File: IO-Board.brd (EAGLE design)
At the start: 160 x 100 mm, 59 parts, among them IC1 PCF8574P, IC2 PCF8574P

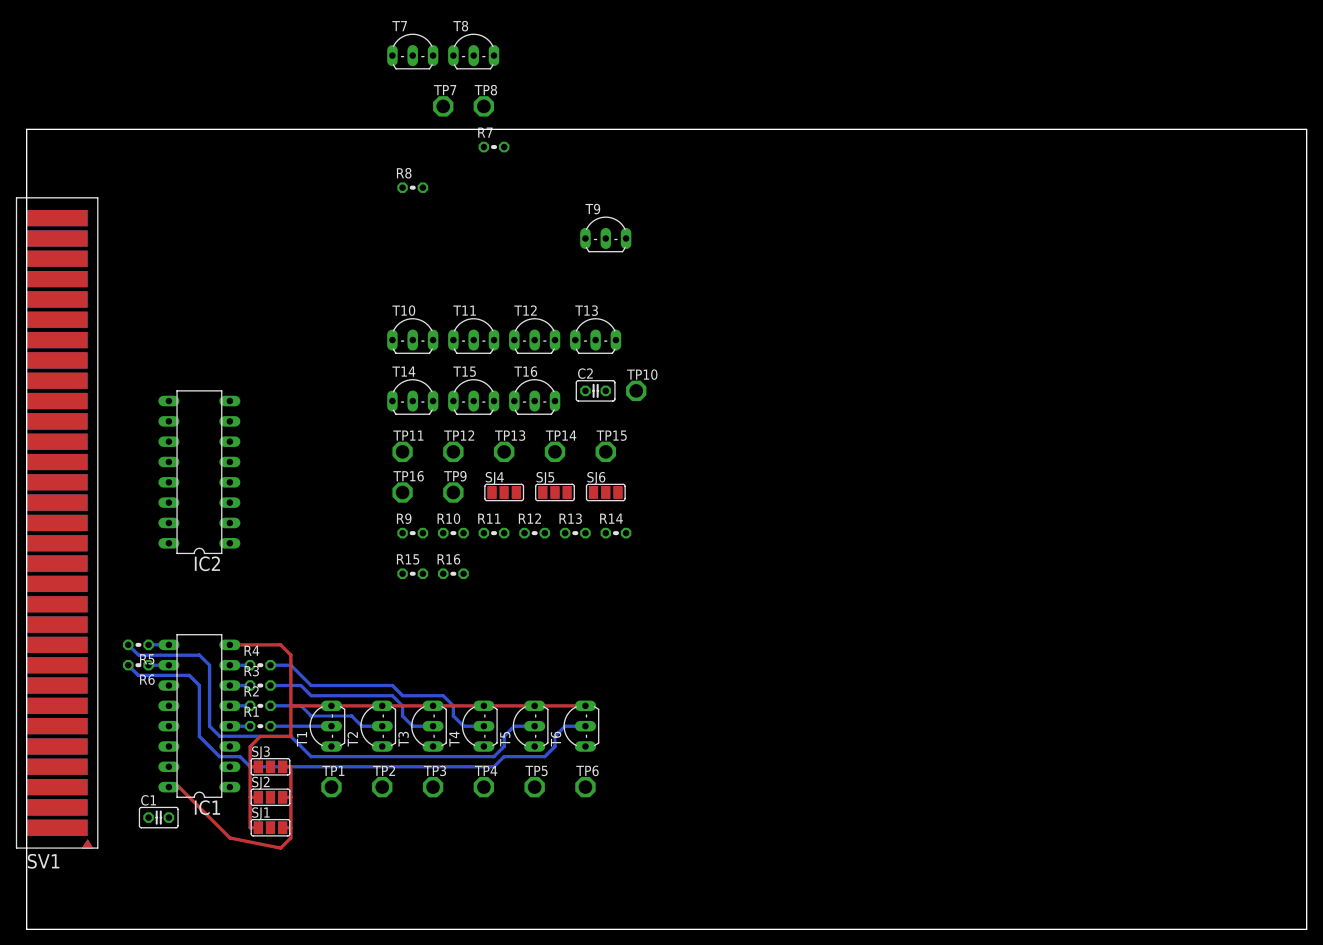
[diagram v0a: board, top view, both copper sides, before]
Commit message: IO-Board angepasst, 433MHz-Sender hinzugefügt
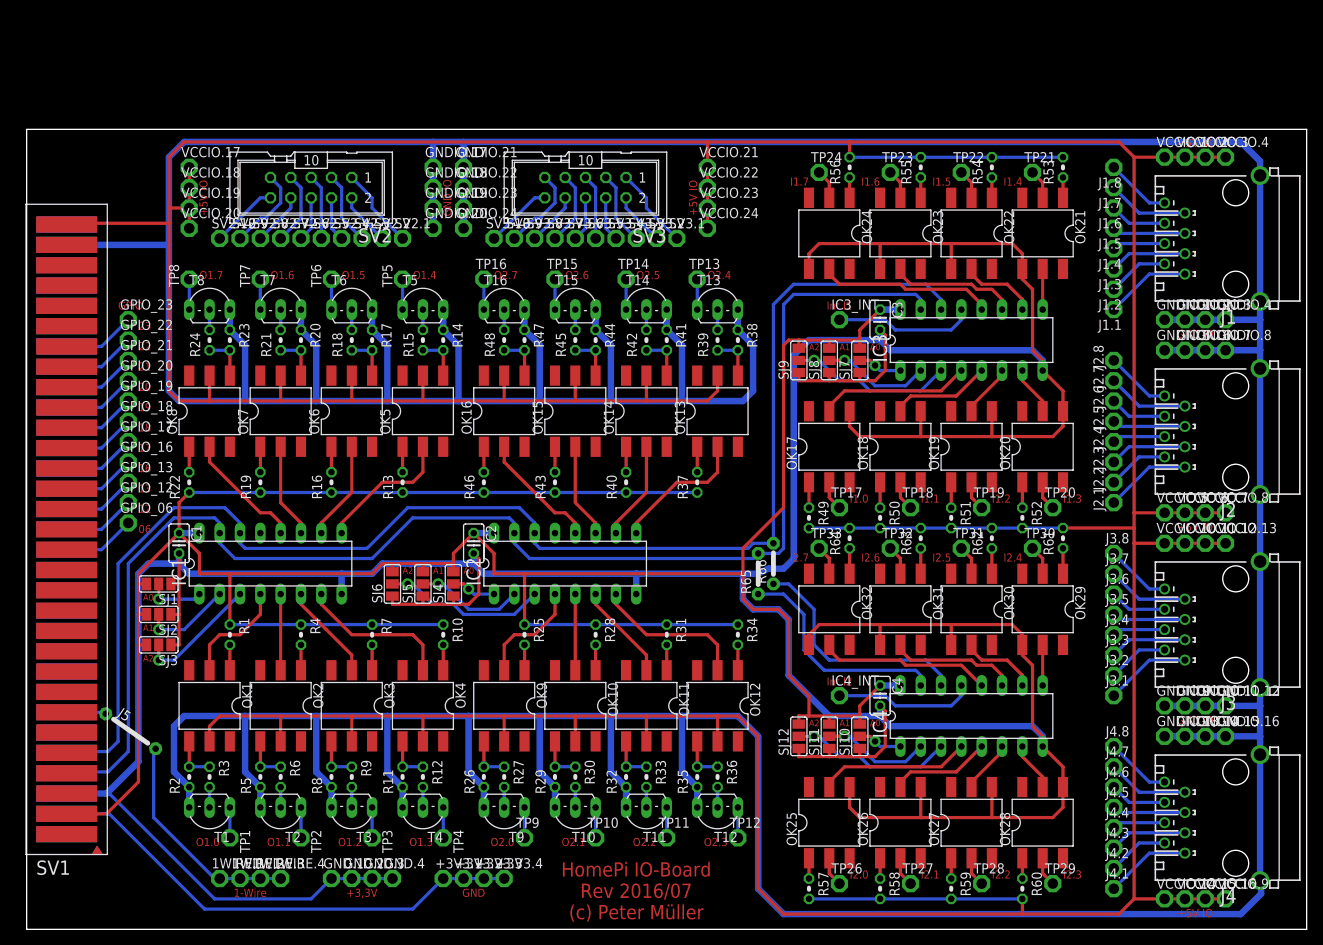
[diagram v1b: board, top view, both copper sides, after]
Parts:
- added +3V3.1, +3V3.2, +3V3.3, +3V3.4, 1WIRE.1, 1WIRE.2, 1WIRE.3, 1WIRE.4, GND.1, GND.2, GND.3, GND.4, GNDIO.1, GNDIO.10, GNDIO.11, GNDIO.12, GNDIO.13, GNDIO.14, GNDIO.15, GNDIO.16, GNDIO.17, GNDIO.18, GNDIO.19, GNDIO.2, GNDIO.20, GNDIO.21, GNDIO.22, GNDIO.23, GNDIO.24, GNDIO.3, GNDIO.4, GNDIO.5, GNDIO.6, GNDIO.7, GNDIO.8, GNDIO.9, GPIO_06, GPIO_12, GPIO_13, GPIO_16, GPIO_17, GPIO_18, GPIO_19, GPIO_20, GPIO_21, GPIO_22, GPIO_23, IC3_INT, IC4_INT, J1.1, J1.2, J1.3, J1.4, J1.5, J1.6, J1.7, J1.8, J2.1, J2.2, J2.3, J2.4, J2.5, J2.6, J2.7, J2.8, J3.1, J3.2, J3.3, J3.4, J3.5, J3.6, J3.7, J3.8, J4.1, J4.2, J4.3, J4.4, J4.5, J4.6, J4.7, J4.8, SV2.1, SV2.10, SV2.2, SV2.3, SV2.4, SV2.5, SV2.6, SV2.7, SV2.8, SV2.9, SV3.1, SV3.10, SV3.2, SV3.3, SV3.4, SV3.5, SV3.6, SV3.7, SV3.8, SV3.9, TP17, TP18, TP19, TP20, TP21, TP22, TP23, TP24, TP26, TP27, TP28, TP29, TP30, TP31, TP32, TP33, VCCIO.1, VCCIO.10, VCCIO.11, VCCIO.12, VCCIO.13, VCCIO.14, VCCIO.15, VCCIO.16, VCCIO.17, VCCIO.18, VCCIO.19, VCCIO.2, VCCIO.20, VCCIO.21, VCCIO.22, VCCIO.23, VCCIO.24, VCCIO.3, VCCIO.4, VCCIO.5, VCCIO.6, VCCIO.7, VCCIO.8, VCCIO.9: TPPAD1-13, testpad:P1-13
- added C3, C4: 100nF, rcl:C025-025X050
- added IC3, IC4: PCF8574P, micro-philips:DIL16
- added J1, J2, J3, J4: (no value), con-amp:555153-1
- added J5: J7MM, jumper:07
- added OK1, OK10, OK11, OK12, OK13, OK14, OK15, OK16, OK17, OK18, OK19, OK2, OK20, OK21, OK22, OK23, OK24, OK25, OK26, OK27, OK28, OK29, OK3, OK30, OK31, OK32, OK4, OK5, OK6, OK7, OK8, OK9: CNY17SMD, homepi:DIL06_SMD
- added R17, R20, R23, R26, R29, R32, R35, R38, R41, R44, R47: 10k, rcl:0204V
- added R18, R21, R24, R27, R30, R33, R36, R39, R42, R45, R48: 4k7, rcl:0204V
- added R19, R22, R25, R28, R31, R34, R37, R40, R43, R46, R49, R50, R51, R52, R53, R54, R55, R56, R57, R58, R59, R60, R61, R62, R63, R64: 330, rcl:0204V
- added R65, R66: J5MM, jumper:05
- added SJ10, SJ11, SJ12, SJ7, SJ8, SJ9: (no value), jumper:SJ_2
- added SV2, SV3: (no value), con-harting-ml:ML10
- R1, R10, R13, R16, R4, R7: value (none) -> 330
- R11, R14, R2, R5, R8: value (none) -> 10k
- R12, R15, R3, R6, R9: value (none) -> 4k7
- T1, T10, T11, T12, T13, T14, T15, T16, T2, T3, T4, T5, T6, T7, T8, T9: value (none) -> BC337-25; device transistor:TO92-EBC -> transistor:TO92-CBE
- TP1, TP10, TP11, TP12, TP13, TP14, TP15, TP16, TP2, TP3, TP4, TP5, TP6, TP7, TP8, TP9: value TPPAD1-17 -> TPPAD1-13; device testpad:P1-17 -> testpad:P1-13
- moved R8 74.4 mm to (38.1, 19.1), turned to 90 degrees
- moved T9 73.5 mm to (59.7, 15.2), turned to 180 degrees
- moved TP6 71.0 mm to (38.1, 81.3), turned to 90 degrees
- moved TP5 65.6 mm to (47.0, 81.3), turned to 90 degrees
- moved T12 63.9 mm to (86.4, 15.2), turned to 180 degrees
- moved T11 63.5 mm to (77.5, 15.2), turned to 180 degrees
- moved T10 63.1 mm to (68.6, 15.2), turned to 180 degrees
- moved R7 62.8 mm to (43.2, 36.8), turned to 270 degrees
- moved TP12 59.9 mm to (88.9, 11.4)
- moved T6 59.1 mm to (40.6, 77.5), turned to 0 degrees
- moved TP11 58.5 mm to (80.0, 11.4)
- moved TP10 56.1 mm to (71.1, 11.4)
- moved T5 53.6 mm to (49.5, 77.5), turned to 0 degrees
- moved IC2 47.1 mm to (67.3, 45.7), turned to 0 degrees
- moved T8 46.7 mm to (22.9, 77.5)
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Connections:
- removed net +5V: SV1.1, SV1.1T
- new net 1WIRE: 1WIRE.1.TP, 1WIRE.2.TP, 1WIRE.3.TP, 1WIRE.4.TP, J5.2
- new net GNDIO: GNDIO.1.TP, GNDIO.10.TP, GNDIO.11.TP, GNDIO.12.TP, GNDIO.13.TP, GNDIO.14.TP, GNDIO.15.TP, GNDIO.16.TP, GNDIO.17.TP, GNDIO.18.TP, GNDIO.19.TP, GNDIO.2.TP, GNDIO.20.TP, GNDIO.21.TP, GNDIO.22.TP, GNDIO.23.TP, GNDIO.24.TP, GNDIO.3.TP, GNDIO.4.TP, GNDIO.5.TP, GNDIO.6.TP, GNDIO.7.TP, GNDIO.8.TP, GNDIO.9.TP, J1.G1, J1.G2, J2.G1, J2.G2, J3.G1, J3.G2, J4.G1, J4.G2, R11.1, R14.1, R17.1, R2.1, R20.1, R23.1, R26.1, R29.1, R32.1, R35.1, R38.1, R41.1, R44.1, R47.1, R5.1, R8.1, SV1.30, SV1.30T, T1.E, T10.E, T11.E, T12.E, T13.E, T14.E, T15.E, T16.E, T2.E, T3.E, T4.E, T5.E, T6.E, T7.E, T8.E, T9.E
- new net IN_1.0: IC3.4, OK17.5
- new net IN_1.1: IC3.5, OK18.5
- new net IN_1.2: IC3.6, OK19.5
- new net IN_1.3: IC3.7, OK20.5
- new net IN_1.4: IC3.9, OK21.5
- new net IN_1.5: IC3.10, OK22.5
- new net IN_1.6: IC3.11, OK23.5
- new net IN_1.7: IC3.12, OK24.5
- new net IN_2.0: IC4.4, OK25.5
- new net IN_2.1: IC4.5, OK26.5
- new net IN_2.2: IC4.6, OK27.5
- new net IN_2.3: IC4.7, OK28.5
- new net IN_2.4: IC4.9, OK29.5
- new net IN_2.5: IC4.10, OK30.5
- new net IN_2.6: IC4.11, OK31.5
- new net IN_2.7: IC4.12, OK32.5
- new net N$100: OK22.1, R54.1
- new net N$101: OK22.2, TP22.TP
- new net N$102: OK23.1, R55.1
- new net N$103: OK23.2, TP23.TP
- new net N$104: OK24.1, R56.1
- new net N$105: OK24.2, TP24.TP
- new net N$106: IC3.13, IC3_INT.TP
- new net N$107: IC4.1, SJ10.2
- new net N$108: IC4.2, SJ11.2
- new net N$109: IC4.3, SJ12.2
- new net N$110: OK25.1, R57.1
- new net N$111: OK25.2, TP26.TP
- new net N$112: OK26.1, R58.1
- new net N$113: OK26.2, TP27.TP
- new net N$114: OK27.1, R59.1
- new net N$115: OK27.2, TP28.TP
- new net N$116: OK28.1, R60.1
- new net N$117: OK28.2, TP29.TP
- new net N$118: OK29.1, R61.1
- new net N$119: OK29.2, TP30.TP
- new net N$120: OK30.1, R62.1
- new net N$121: OK30.2, TP31.TP
- new net N$122: OK31.1, R63.1
- new net N$123: OK31.2, TP32.TP
- new net N$124: OK32.1, R64.1
- new net N$125: OK32.2, TP33.TP
- new net N$126: IC4.13, IC4_INT.TP
- new net N$127: IC4.15, R65.1
- new net N$128: IC4.14, R66.1
- new net N$129: J3.1, J3.1.TP
- new net N$130: J3.2, J3.2.TP
- new net N$131: J3.3, J3.3.TP
- new net N$132: J3.4, J3.4.TP
- new net N$133: J3.5, J3.5.TP
- new net N$134: J3.6, J3.6.TP
- new net N$135: J3.7, J3.7.TP
- new net N$136: J3.8, J3.8.TP
- new net N$137: J4.1, J4.1.TP
- new net N$138: J4.2, J4.2.TP
- new net N$139: J4.3, J4.3.TP
- new net N$140: J4.4, J4.4.TP
- new net N$141: J4.5, J4.5.TP
- new net N$142: J4.6, J4.6.TP
- new net N$143: J4.7, J4.7.TP
- new net N$144: J4.8, J4.8.TP
- new net N$145: J5.1, SV1.7, SV1.7T
- new net N$146: GPIO_23.TP, SV1.25, SV1.25T
- new net N$147: GPIO_22.TP, SV1.24, SV1.24T
- new net N$148: GPIO_21.TP, SV1.23, SV1.23T
- new net N$149: GPIO_20.TP, SV1.22, SV1.22T
- new net N$150: GPIO_19.TP, SV1.21, SV1.21T
- new net N$151: GPIO_18.TP, SV1.20, SV1.20T
- new net N$152: GPIO_17.TP, SV1.19, SV1.19T
- new net N$153: GPIO_16.TP, SV1.18, SV1.18T
- new net N$154: GPIO_13.TP, SV1.17, SV1.17T
- new net N$155: GPIO_12.TP, SV1.16, SV1.16T
- new net N$156: GPIO_06.TP, SV1.15, SV1.15T
- new net N$157: SV2.1, SV2.1.TP
- new net N$158: SV2.2, SV2.2.TP
- new net N$159: SV2.3, SV2.3.TP
- new net N$160: SV2.4, SV2.4.TP
- new net N$161: SV2.5, SV2.5.TP
- new net N$162: SV2.6, SV2.6.TP
- new net N$163: SV2.7, SV2.7.TP
- new net N$164: SV2.8, SV2.8.TP
- new net N$165: SV2.9, SV2.9.TP
- new net N$166: SV2.10, SV2.10.TP
- new net N$167: SV3.1, SV3.1.TP
- new net N$168: SV3.2, SV3.2.TP
- new net N$169: SV3.3, SV3.3.TP
- new net N$170: SV3.4, SV3.4.TP
- new net N$171: SV3.5, SV3.5.TP
- new net N$172: SV3.6, SV3.6.TP
- new net N$173: SV3.7, SV3.7.TP
- new net N$174: SV3.8, SV3.8.TP
- new net N$175: SV3.9, SV3.9.TP
- new net N$176: SV3.10, SV3.10.TP
- new net N$28: T7.C, TP7.TP
- new net N$29: OK7.1, R19.2
- new net N$30: OK7.4, R20.2, R21.1
- new net N$55: R27.2, T9.B
- new net N$56: T10.C, TP10.TP
- new net N$57: OK10.1, R28.2
- new net N$58: OK10.4, R29.2, R30.1
- new net N$59: R30.2, T10.B
- new net N$60: T11.C, TP11.TP
- new net N$61: OK11.1, R31.2
- new net N$62: OK11.4, R32.2, R33.1
- new net N$63: R33.2, T11.B
- new net N$64: T12.C, TP12.TP
- new net N$65: OK12.1, R34.2
- new net N$66: OK12.4, R35.2, R36.1
- new net N$67: R36.2, T12.B
- new net N$68: T13.C, TP13.TP
- new net N$69: OK13.1, R37.2
- new net N$70: OK13.4, R38.2, R39.1
- new net N$71: R39.2, T13.B
- new net N$72: T14.C, TP14.TP
- new net N$73: OK14.1, R40.2
- new net N$74: OK14.4, R41.2, R42.1
- new net N$75: R42.2, T14.B
- new net N$76: T15.C, TP15.TP
- new net N$77: OK15.1, R43.2
- new net N$78: OK15.4, R44.2, R45.1
- new net N$79: R45.2, T15.B
- new net N$80: T16.C, TP16.TP
- new net N$81: OK16.1, R46.2
- new net N$82: OK16.4, R47.2, R48.1
- new net N$83: R48.2, T16.B
- new net N$87: IC3.1, SJ7.2
- new net N$88: IC3.2, SJ8.2
- new net N$89: IC3.3, SJ9.2
- new net N$90: OK17.1, R49.1
- new net N$91: OK17.2, TP17.TP
- new net N$92: OK18.1, R50.1
- new net N$93: OK18.2, TP18.TP
- new net N$94: OK19.1, R51.1
- new net N$95: OK19.2, TP19.TP
- new net N$96: OK20.1, R52.1
- new net N$97: OK20.2, TP20.TP
- new net N$98: OK21.1, R53.1
- new net N$99: OK21.2, TP21.TP
- new net OUT_1.0: IC1.4, OK1.2
- new net OUT_1.1: IC1.5, OK2.2
- new net OUT_1.2: IC1.6, OK3.2
- new net OUT_1.3: IC1.7, OK4.2
- new net OUT_1.4: IC1.9, OK5.2
- new net OUT_1.5: IC1.10, OK6.2
- new net OUT_1.6: IC1.11, OK7.2
- new net OUT_1.7: IC1.12, OK8.2
- new net OUT_2.0: IC2.4, OK9.2
- new net OUT_2.1: IC2.5, OK10.2
- new net OUT_2.2: IC2.6, OK11.2
- new net OUT_2.3: IC2.7, OK12.2
- new net OUT_2.4: IC2.9, OK13.2
- new net OUT_2.5: IC2.10, OK14.2
- new net OUT_2.6: IC2.11, OK15.2
- new net OUT_2.7: IC2.12, OK16.2
- new net VCCIO: OK1.5, OK10.5, OK11.5, OK12.5, OK13.5, OK14.5, OK15.5, OK16.5, OK2.5, OK3.5, OK4.5, OK5.5, OK6.5, OK7.5, OK8.5, OK9.5, R49.2, R50.2, R51.2, R52.2, R53.2, R54.2, R55.2, R56.2, R57.2, R58.2, R59.2, R60.2, R61.2, R62.2, R63.2, R64.2, SV1.31, SV1.31T, VCCIO.1.TP, VCCIO.10.TP, VCCIO.11.TP, VCCIO.12.TP, VCCIO.13.TP, VCCIO.14.TP, VCCIO.15.TP, VCCIO.16.TP, VCCIO.17.TP, VCCIO.18.TP, VCCIO.19.TP, VCCIO.2.TP, VCCIO.20.TP, VCCIO.21.TP, VCCIO.22.TP, VCCIO.23.TP, VCCIO.24.TP, VCCIO.3.TP, VCCIO.4.TP, VCCIO.5.TP, VCCIO.6.TP, VCCIO.7.TP, VCCIO.8.TP, VCCIO.9.TP
- net +3V3: now also +3V3.1.TP, +3V3.2.TP, +3V3.3.TP, +3V3.4.TP, C3.1, C4.1, IC3.16, IC4.16, R1.1, R10.1, R13.1, R16.1, R19.1, R22.1, R25.1, R28.1, R31.1, R34.1, R37.1, R4.1, R40.1, R43.1, R46.1, R7.1, SJ10.3, SJ11.3, SJ12.3, SJ7.3, SJ8.3, SJ9.3
- net GND: now also C3.2, C4.2, GND.1.TP, GND.2.TP, GND.3.TP, GND.4.TP, IC3.8, IC4.8, OK17.4, OK18.4, OK19.4, OK20.4, OK21.4, OK22.4, OK23.4, OK24.4, OK25.4, OK26.4, OK27.4, OK28.4, OK29.4, OK30.4, OK31.4, OK32.4, SJ10.1, SJ11.1, SJ12.1, SJ7.1, SJ8.1, SJ9.1; no longer T1.C, T10.C, T11.C, T12.C, T13.C, T14.C, T15.C, T16.C, T2.C, T3.C, T4.C, T5.C, T6.C, T7.C, T8.C, T9.C
- net N$10: now also OK2.4, R5.2, R6.1; no longer T3.E, TP3.TP
- net N$11: now also R6.2, T2.B; no longer T4.E, TP4.TP
- net N$12: now also T3.C, TP3.TP; no longer R6.2, T6.B
- net N$13: now also OK3.1, R7.2; no longer R5.2, T5.B
- net N$14: now also OK3.4, R8.2, R9.1; no longer R4.2, T4.B
- net N$15: now also R9.2; no longer R3.2
- net N$16: now also T4.C, TP4.TP; no longer T7.E, TP7.TP
- net N$17: now also OK4.1, R10.2; no longer T8.E, TP8.TP
- net N$18: now also OK4.4, R11.2, R12.1; no longer R8.2, T8.B
- net N$19: now also R12.2, T4.B; no longer R7.2, T7.B
- net N$20: now also T5.C, TP5.TP; no longer IC1.4, R1.1
- net N$21: now also OK5.1, R13.2; no longer IC1.5, R2.1
- net N$22: now also OK5.4, R14.2, R15.1; no longer IC1.6, R3.1
- net N$23: now also R15.2, T5.B; no longer IC1.7, R4.1
- net N$24: now also T6.C, TP6.TP; no longer IC1.9, R5.1
- net N$25: now also OK6.1, R16.2; no longer IC1.10, R6.1
- net N$26: now also OK6.4, R17.2, R18.1; no longer IC1.11, R7.1
- net N$27: now also R18.2, T6.B; no longer IC1.12, R8.1
- net N$31: now also R21.2, T7.B; no longer T9.E, TP9.TP
- net N$32: now also T8.C, TP8.TP; no longer T10.E, TP10.TP
- net N$33: now also OK8.1, R22.2; no longer R10.2, T10.B
- net N$34: now also OK8.4, R23.2, R24.1; no longer R9.2, T9.B
- net N$35: now also R24.2, T8.B; no longer T11.E, TP11.TP
- net N$36: now also J1.1, J1.1.TP; no longer T12.E, TP12.TP
- net N$37: now also J1.2, J1.2.TP; no longer R12.2, T12.B
- net N$38: now also J1.3, J1.3.TP; no longer R11.2, T11.B
- net N$39: now also J1.4, J1.4.TP; no longer T13.E, TP13.TP
- net N$4: now also T1.C; no longer T1.E
- net N$40: now also J1.5, J1.5.TP; no longer T14.E, TP14.TP
- net N$41: now also J1.6, J1.6.TP; no longer R14.2, T14.B
- net N$42: now also J1.7, J1.7.TP; no longer R13.2, T13.B
- net N$43: now also J1.8, J1.8.TP; no longer T15.E, TP15.TP
- net N$44: now also J2.1, J2.1.TP; no longer T16.E, TP16.TP
- net N$45: now also J2.2, J2.2.TP; no longer R16.2, T16.B
- net N$46: now also J2.3, J2.3.TP; no longer R15.2, T15.B
- net N$47: now also J2.4, J2.4.TP; no longer IC2.4, R9.1
- net N$48: now also J2.5, J2.5.TP; no longer IC2.5, R10.1
- net N$49: now also J2.6, J2.6.TP; no longer IC2.6, R11.1
- net N$5: now also OK1.1, R1.2; no longer T2.E, TP2.TP
- net N$50: now also J2.7, J2.7.TP; no longer IC2.7, R12.1
- net N$51: now also J2.8, J2.8.TP; no longer IC2.9, R13.1
- net N$52: now also T9.C, TP9.TP; no longer IC2.10, R14.1
- net N$53: now also OK9.1, R25.2; no longer IC2.11, R15.1
- net N$54: now also OK9.4, R26.2, R27.1; no longer IC2.12, R16.1
- net N$6: now also OK1.4, R2.2, R3.1; no longer T5.E, TP5.TP
- net N$7: now also R3.2, T1.B; no longer T6.E, TP6.TP
- net N$8: now also T2.C, TP2.TP; no longer R2.2, T2.B
- net N$9: now also OK2.1, R4.2; no longer R1.2, T1.B
- net SCL: now also IC3.14, R66.2
- net SDA: now also IC3.15, R65.2
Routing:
- net GNDIO: track 0.00 -> 767.1 mm
- net VCCIO: track 0.00 -> 677.7 mm
- net GND: track 74.0 -> 553.8 mm
- net +3V3: track 30.5 -> 424.9 mm
- net SCL: track 0.00 -> 177.5 mm
- net SDA: track 0.00 -> 176.1 mm
- net N$12: track 69.0 -> 3.81 mm
- net N$13: track 63.4 -> 3.18 mm
- net N$128: track 0.00 -> 29.6 mm
- net N$127: track 0.00 -> 28.4 mm
- net 1WIRE: track 0.00 -> 27.7 mm
- net N$14: track 30.6 -> 5.71 mm
- net IN_1.7: track 0.00 -> 21.9 mm
- net IN_2.7: track 0.00 -> 21.5 mm
- net N$15: track 23.2 -> 2.54 mm
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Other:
- board text added: "+3,3V"
- board text added: "+5V IO"
- board text added: "06"
- board text added: "1-Wire"
- board text added: "12"
- board text added: "13"
- board text added: "16"
- board text added: "17"
- board text added: "18"
- board text added: "19"
- board text added: "20"
- board text added: "21"
- board text added: "22"
- board text added: "23"
- board text added: "A0"
- board text added: "A1"
- board text added: "A2"
- board text added: "GND"
- board text added: "GND IO"
- board text added: "GPIO"
- board text added: "HomePi IO-Board Rev 2016/07 (c) Peter Müller"
- board text added: "I1.0"
- board text added: "I1.1"
- board text added: "I1.2"
- board text added: "I1.3"
- board text added: "I1.4"
- board text added: "I1.5"
- board text added: "I1.6"
- board text added: "I1.7"
- board text added: "I2.0"
- board text added: "I2.1"
- board text added: "I2.2"
- board text added: "I2.3"
- board text added: "I2.4"
- board text added: "I2.5"
- board text added: "I2.6"
- board text added: "I2.7"
- board text added: "Int I1"
- board text added: "Int I2"
- board text added: "O1.0"
- board text added: "O1.1"
- board text added: "O1.2"
- board text added: "O1.3"
- board text added: "O1.4"
- board text added: "O1.5"
- board text added: "O1.6"
- board text added: "O1.7"
- board text added: "O2.0"
- board text added: "O2.1"
- board text added: "O2.2"
- board text added: "O2.3"
- board text added: "O2.4"
- board text added: "O2.5"
- board text added: "O2.6"
- board text added: "O2.7"
